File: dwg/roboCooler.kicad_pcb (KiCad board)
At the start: 2 copper layers, 82 parts, among them J1 CONN_01X02, J10 CONN_02X03, J11 CONN_02X03, J13 CONN_02X03, J14 CONN_02X03, J2 CONN_01X02, J3 CONN_02X05, J4 CONN_01X06, J5 CONN_01X12, J7 CONN_02X03, J8 CONN_02X03, Q1 NMOS, Q2 NMOS, SW1 TL3342, U1 SN74LV, U2 TB6549, U3 STM32F407VGTx, Y1 8MHz

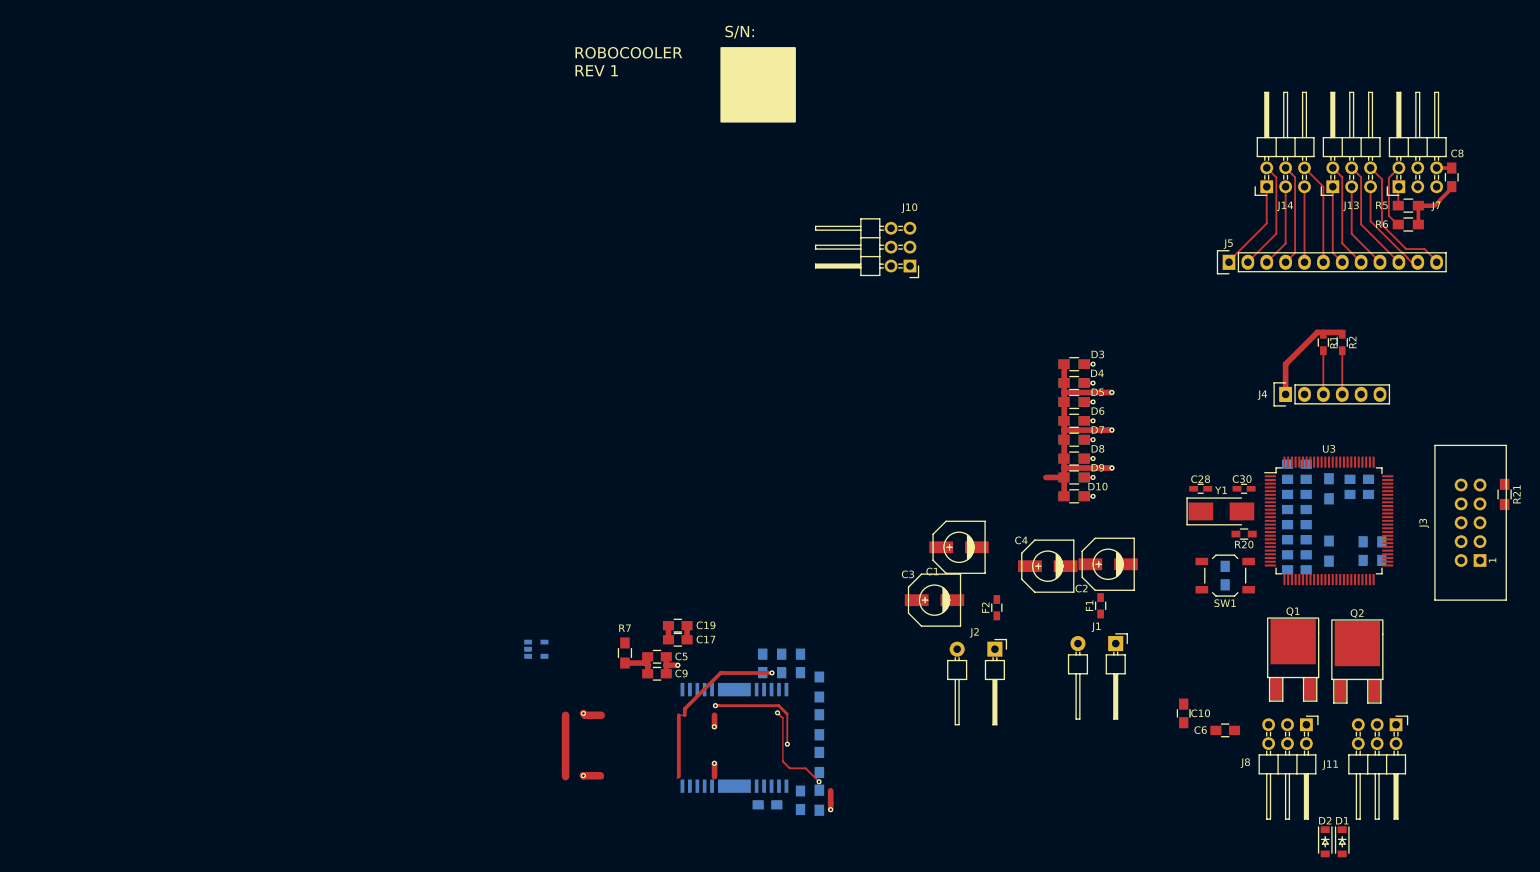
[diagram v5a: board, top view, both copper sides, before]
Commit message: updated placement on new board. No DRC errors
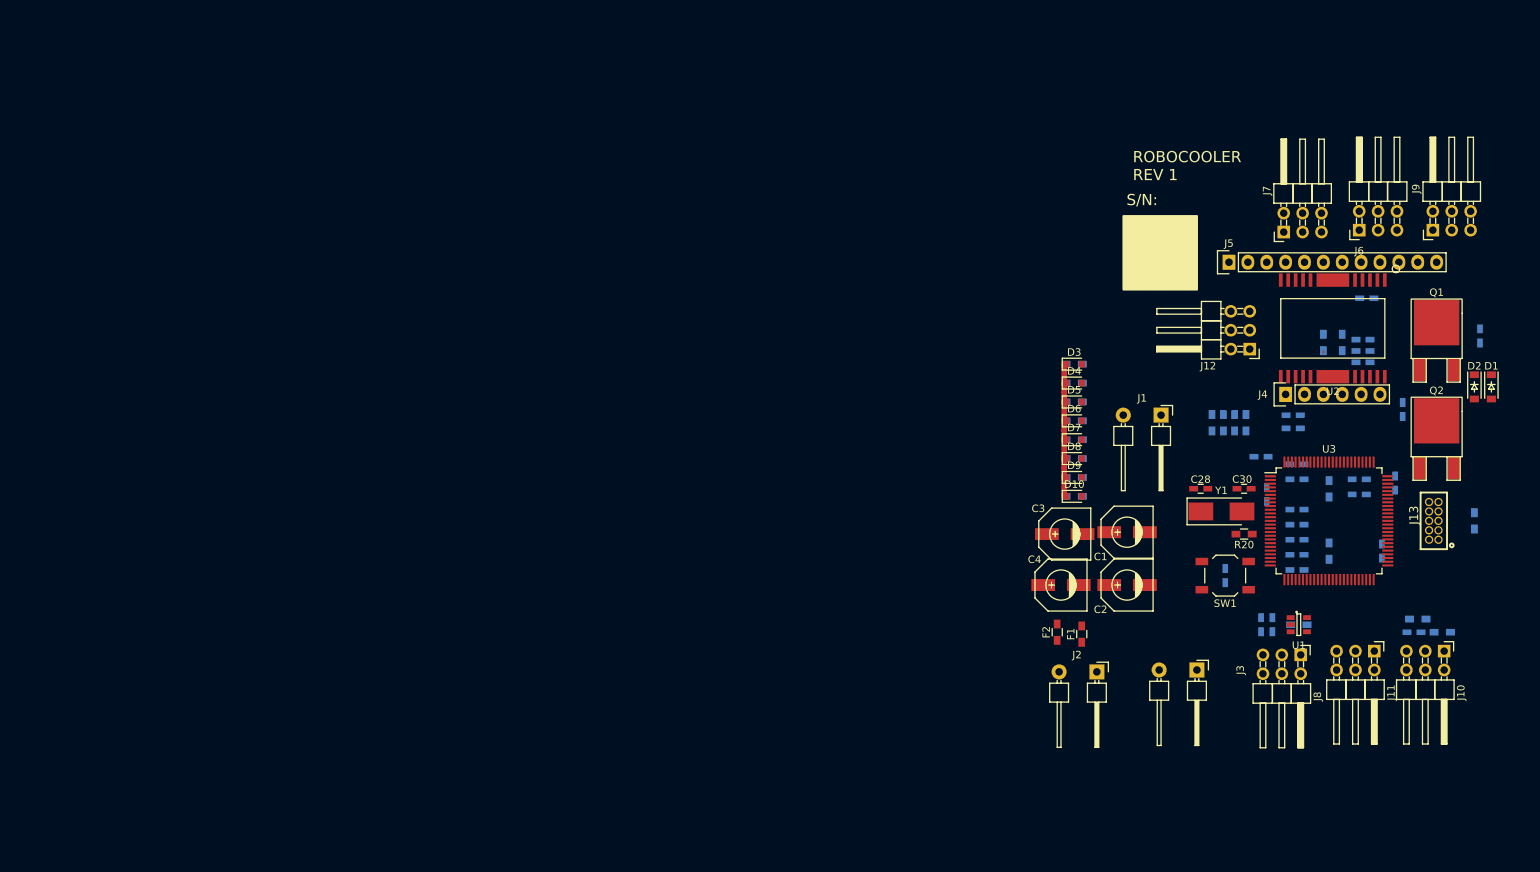
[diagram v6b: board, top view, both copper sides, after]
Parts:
- removed J14: CONN_02X03, Pin_Headers:Pin_Header_Angled_2x03
- added J12: CONN_02X03, Pin_Headers:Pin_Header_Angled_2x03_Pitch2.54mm, F.Cu at (187.7, 59.9)
- added J6: CONN_02X03, Pin_Headers:Pin_Header_Angled_2x03_Pitch2.54mm, F.Cu at (202.4, 43.9)
- added J9: CONN_02X03, Pin_Headers:Pin_Header_Angled_2x03_Pitch2.54mm, F.Cu at (212.3, 43.9)
- C1, C2, C3, C4: value 100uF -> 100UF
- C10: value 1UF -> .01UF; footprint Capacitors_SMD:C_0805_HandSoldering -> Capacitors_SMD:C_0603_HandSoldering; moved to B.Cu
- C11: value 2.2uF -> 1UF; footprint Capacitors_SMD:C_0805_HandSoldering -> Capacitors_SMD:C_0603_HandSoldering
- C12: value 10uF -> .22UF; footprint Capacitors_SMD:C_0805_HandSoldering -> Capacitors_SMD:C_0603_HandSoldering
- C13, C15: value 0.22UF -> .22UF; footprint Capacitors_SMD:C_0805_HandSoldering -> Capacitors_SMD:C_0603_HandSoldering
- C14: value 0.22UF -> .01UF; footprint Capacitors_SMD:C_0805_HandSoldering -> Capacitors_SMD:C_0603_HandSoldering
- C16, C20, C21, C22, C23, C24, C25, C26, C27, C29, C31: footprint Capacitors_SMD:C_0805_HandSoldering -> Capacitors_SMD:C_0603_HandSoldering
- C17: value .01UF -> 0.1uF; footprint Capacitors_SMD:C_0805_HandSoldering -> Capacitors_SMD:C_0603_HandSoldering; moved to B.Cu
- C18: value .01UF -> 2.2uF; footprint Capacitors_SMD:C_0805_HandSoldering -> Capacitors_SMD:C_0603_HandSoldering
- C19: value 1UF -> 10uF; footprint Capacitors_SMD:C_0805_HandSoldering -> Capacitors_SMD:C_0603_HandSoldering; moved to B.Cu
- C5: footprint Capacitors_SMD:C_0805_HandSoldering -> Capacitors_SMD:C_0603_HandSoldering; moved to B.Cu
- C6: value .01UF -> 1UF; footprint Capacitors_SMD:C_0805_HandSoldering -> Capacitors_SMD:C_0603_HandSoldering; moved to B.Cu
- C7: value 0.1uF -> .01UF; footprint Capacitors_SMD:C_0805_HandSoldering -> Capacitors_SMD:C_0603_HandSoldering
- C8: value .1UF -> 1UF; footprint Capacitors_SMD:C_0805_HandSoldering -> Capacitors_SMD:C_0603_HandSoldering; moved to B.Cu
- C9: value 1UF -> .1UF; footprint Capacitors_SMD:C_0805_HandSoldering -> Capacitors_SMD:C_0603_HandSoldering; moved to B.Cu
- D10, D3, D4, D5, D6, D7, D8, D9: value Led_Small -> LED_Small; footprint Resistors_SMD:R_0805_HandSoldering -> Diodes_SMD:D_0805
- F1, F2: value PTC -> 3.5A
- J10, J11, J7, J8: footprint Pin_Headers:Pin_Header_Angled_2x03 -> Pin_Headers:Pin_Header_Angled_2x03_Pitch2.54mm
- J13: value CONN_02X03 -> 3221-10-0100-00; footprint Pin_Headers:Pin_Header_Angled_2x03 -> roboCooler:Header_02x05_50mil
- J3: value CONN_02X05 -> CONN_01X02; footprint Connectors:IDC_Header_Straight_10pins -> roboCooler:Pin_Header_Angled_1x02_200mil
- R1, R2: value 10k -> 10K; moved to B.Cu
- R10, R8: value 10k -> 10K; footprint Resistors_SMD:R_0805_HandSoldering -> Resistors_SMD:R_0603_HandSoldering
- R11, R9: value 10k -> 200; footprint Resistors_SMD:R_0805_HandSoldering -> Resistors_SMD:R_0603_HandSoldering
- R12, R13, R14, R15, R16, R17, R18, R19: footprint Resistors_SMD:R_0805_HandSoldering -> Resistors_SMD:R_0603_HandSoldering
- R21, R5: footprint Resistors_SMD:R_0805_HandSoldering -> Resistors_SMD:R_0603_HandSoldering; moved to B.Cu
- R3: value 200 -> 1K; footprint Resistors_SMD:R_0805_HandSoldering -> Resistors_SMD:R_0603_HandSoldering
- R4: value 200 -> 1k; footprint Resistors_SMD:R_0805_HandSoldering -> Resistors_SMD:R_0603_HandSoldering
- R6, R7: value 1k -> 10K; footprint Resistors_SMD:R_0805_HandSoldering -> Resistors_SMD:R_0603_HandSoldering; moved to B.Cu
- U1: value SN74LV -> 74AHC1G14; moved to F.Cu
- U2: moved to F.Cu
- moved U1 102.7 mm to (194.3, 97.0)
- moved C9 102.0 mm to (209.8, 98.0)
- moved C13 101.8 mm to (203.5, 53.1), turned to 180 degrees
- moved C14 99.8 mm to (202.9, 61.7)
- moved U2 97.0 mm to (198.9, 57.7)
- moved C5 91.6 mm to (193.5, 68.8)
- moved C15 89.5 mm to (202.9, 58.7), turned to 180 degrees
- moved J10 88.6 mm to (213.9, 100.6), turned to 270 degrees
- moved C18 88.5 mm to (207.3, 78.0)
- moved C16 86.6 mm to (202.9, 60.2), turned to 180 degrees
- moved R7 86.3 mm to (184.2, 69.8), turned to 270 degrees
- moved C19 81.7 mm to (189.2, 74.4)
- moved C17 81.6 mm to (190.0, 79.5), turned to 90 degrees
- moved R10 73.4 mm to (187.2, 69.8), turned to 270 degrees
- moved R8 66.2 mm to (185.7, 69.8)
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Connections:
- net JTRST renamed Net-(U3-Pad90)
- C11 pad 1: Net-(C11-Pad1) -> +12V
- C12 pad 1: VDD -> Net-(C12-Pad1)
- C13 pad 2: GND -> Net-(C13-Pad2)
- C14 pad 2: Net-(C14-Pad2) -> GND
- C15 pad 1: GND -> +12V
- C15 pad 2: +12V -> GND
- C16 pad 1: GND -> +12V
- C16 pad 2: +12V -> GND
- C17 pad 1: +3V3 -> VCC
- C18 pad 1: Net-(C18-Pad1) -> VCAP_2
- C19 pad 1: +3V3 -> VCC
- C20 pad 1: Net-(C20-Pad1) -> VCAP_1
- C22 pad 1: VDD -> VCC
- C23 pad 1: VDD -> VCC
- C24 pad 1: VDD -> VCC
- C25 pad 1: VDD -> VCC
- C26 pad 1: VDD -> VCC
- C27 pad 1: VDD -> VCC
- C5 pad 1: +5V -> +3V3
- C6 pad 1: +12V -> +3V3
- C7 pad 1: VDD -> +5V
- C8 pad 1: +5P -> +5V
- J1 pad 1: Net-(F1-Pad1) -> +3V3
- J10 pad 1: +5V -> Net-(J10-Pad1)
- J10 pad 2: +5V -> Net-(J10-Pad2)
- J10 pad 3: Net-(J10-Pad3) -> HALL_1
- J10 pad 4: Net-(J10-Pad3) -> HALL_2
- J11 pad 1: MOTOR_OUT1 -> Net-(J11-Pad1)
- J11 pad 2: MOTOR_OUT1 -> Net-(J11-Pad2)
- J11 pad 3: GND -> PUSH_1
- J11 pad 4: GND -> PUSH_2
- J11 pad 5: MOTOR_OUT2 -> GND
- J11 pad 6: MOTOR_OUT2 -> GND
- J13 pad 1: CS_5 -> VCC
- J13 pad 2: CS_4 -> JTMS/SWDIO
- J13 pad 3: CS_3 -> GND
- J13 pad 4: CS_2 -> JTCK/SWCLK
- J13 pad 5: CS_1 -> GND
- J13 pad 6: CS_0 -> JTDO/SWO
- J2 pad 1: Net-(F2-Pad1) -> Net-(F1-Pad1)
- J3 pad 1: VCC -> Net-(F2-Pad1)
- J3 pad 2: JTMS/SWDIO -> GND
- J7 pad 1: Net-(J7-Pad1) -> CS_11
- J7 pad 2: Net-(J7-Pad2) -> CS_10
- J7 pad 3: HALL_1 -> CS_9
- J7 pad 4: HALL_2 -> CS_8
- J7 pad 5: GND -> CS_7
- J7 pad 6: GND -> CS_6
- J8 pad 1: +12V -> +5V
- J8 pad 2: +12V -> +5V
- J8 pad 4: Net-(J8-Pad4) -> Net-(J8-Pad3)
- J8 pad 5: Net-(D1-Pad2) -> GND
- J8 pad 6: Net-(D2-Pad2) -> GND
- R10 pad 1: GND -> MOTOR_SB
- R10 pad 2: MOTOR_PWM -> GND
- R11 pad 1: GND -> LED_1
- R11 pad 2: MOTOR_SB -> Net-(D4-Pad2)
- R21 pad 2: Net-(J3-Pad7) -> Net-(J13-Pad7)
- R3 pad 1: LED_0 -> +5V
- R3 pad 2: Net-(D3-Pad2) -> Net-(J8-Pad3)
- R4 pad 1: LED_1 -> Net-(J10-Pad1)
- R4 pad 2: Net-(D4-Pad2) -> +5V
- R5 pad 1: Net-(J7-Pad1) -> +5V
- R5 pad 2: +5P -> Net-(J10-Pad2)
- R6 pad 1: Net-(J7-Pad2) -> MOTOR_FWD
- R6 pad 2: +5P -> GND
- R7 pad 1: +5V -> MOTOR_REV
- R7 pad 2: Net-(J10-Pad3) -> GND
- R8 pad 1: GND -> MOTOR_PWM
- R8 pad 2: MOTOR_IN1 -> GND
- R9 pad 1: GND -> LED_0
- R9 pad 2: MOTOR_IN2 -> Net-(D3-Pad2)
- U1 pad 4: Net-(J10-Pad3) -> Net-(J8-Pad3)
- U2 pad 18: Net-(C18-Pad1) -> Net-(C14-Pad1)
- U2 pad 2: Net-(C13-Pad1) -> Net-(C12-Pad1)
- U2 pad 3: Net-(C14-Pad1) -> Net-(C13-Pad1)
- U2 pad 4: Net-(C14-Pad2) -> Net-(C13-Pad2)
- U2 pad 7: MOTOR_IN1 -> MOTOR_FWD
- U2 pad 8: MOTOR_IN2 -> MOTOR_REV
- U3 pad 100: VDD -> VCC
- U3 pad 11: VDD -> VCC
- U3 pad 19: VDD -> VCC
- U3 pad 24: /mcu/LED_1 -> LED_1
- U3 pad 25: /mcu/LED_UART -> LED_UART
- U3 pad 26: /mcu/LED_2 -> LED_2
- U3 pad 28: VDD -> VCC
- U3 pad 32: /mcu/LED_3 -> LED_3
- U3 pad 34: /mcu/LED_4 -> LED_4
- U3 pad 36: /mcu/LED_5 -> LED_5
- U3 pad 38: /mcu/LED_6 -> LED_6
- U3 pad 4: /mcu/PUSH_1 -> PUSH_1
- U3 pad 40: /mcu/LED_7 -> LED_7
- U3 pad 49: Net-(C11-Pad1) -> VCAP_1
- U3 pad 50: VDD -> VCC
- U3 pad 6: VDD -> VCC
- U3 pad 63: /mcu/FAN_PWM -> FAN
- U3 pad 66: /mcu/PUMP_PWM -> PUMP
- U3 pad 67: /mcu/MOTOR_PWM -> MOTOR_PWM
- U3 pad 7: /mcu/PUSH_2 -> PUSH_2
- U3 pad 73: Net-(C20-Pad1) -> VCAP_2
- U3 pad 75: VDD -> VCC
- U3 pad 79: /mcu/MOTOR_REV -> MOTOR_REV
- U3 pad 81: /mcu/MOTOR_FWD -> MOTOR_FWD
- U3 pad 83: /mcu/MOTOR_SB -> MOTOR_SB
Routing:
- net (no net): track 70.1 -> 0.12 mm, vias 10 -> 0
- net GND: track 47.3 -> 17.8 mm, vias 4 -> 0
- net CS_0: track 17.8 -> 0.15 mm
- net +3V3: track 15.4 -> 0.00 mm
- net CS_2: track 15.3 -> 0.01 mm
- net CS_10: track 14.8 -> 0.01 mm
- net CS_4: track 14.3 -> 0.00 mm
- net CS_6: track 13.8 -> 0.00 mm
- net CS_8: track 13.8 -> 0.02 mm
- net CS_1: track 13.3 -> 0.83 mm
- net CS_11: track 12.3 -> 0.15 mm
- net CS_3: track 11.7 -> 0.01 mm
- net CS_9: track 11.2 -> 0.02 mm
- net CS_5: track 10.7 -> 0.00 mm
- net +5P: track 10.2 -> 0.00 mm
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
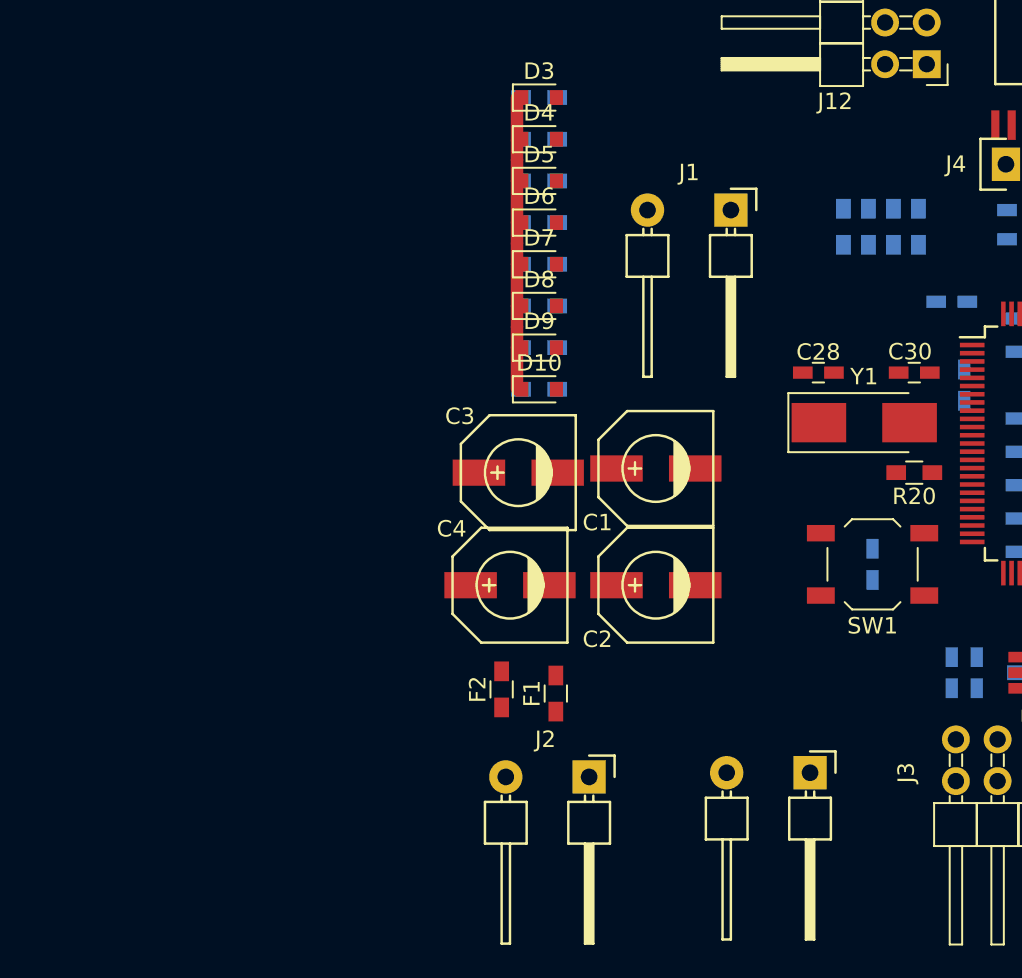
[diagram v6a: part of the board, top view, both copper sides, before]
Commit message: added 5V switcher
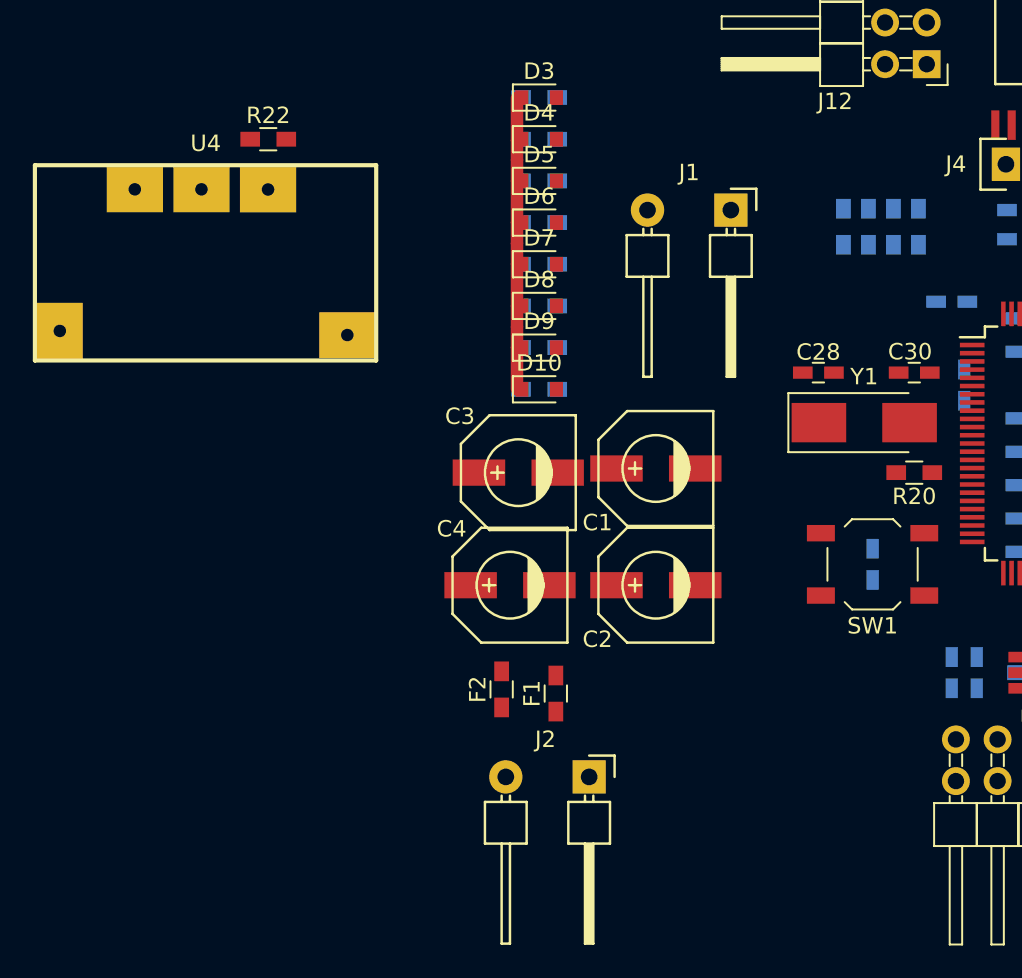
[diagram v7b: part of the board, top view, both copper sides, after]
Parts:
- removed J3: CONN_01X02, roboCooler:Pin_Header_Angled_1x02_200mil
- added R22: 10K, Resistors_SMD:R_0603_HandSoldering, F.Cu at (147.6, 64.5)
- added U4: OKY-T/3-D12N-C, roboCooler:OKY-T3, F.Cu at (134.9, 76.2)
- F2: value 3.5A -> 5A
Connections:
- C2 pad 1: +5V -> Net-(C2-Pad1)
- C4 pad 1: +5V -> Net-(C2-Pad1)
- F2 pad 1: Net-(F2-Pad1) -> +5V
- F2 pad 2: +5V -> Net-(C2-Pad1)
- J11 pad 3: PUSH_1 -> Net-(J11-Pad3)
- J11 pad 4: PUSH_2 -> Net-(J11-Pad4)
- J11 pad 5: GND -> Net-(J11-Pad5)
- J11 pad 6: GND -> Net-(J11-Pad6)

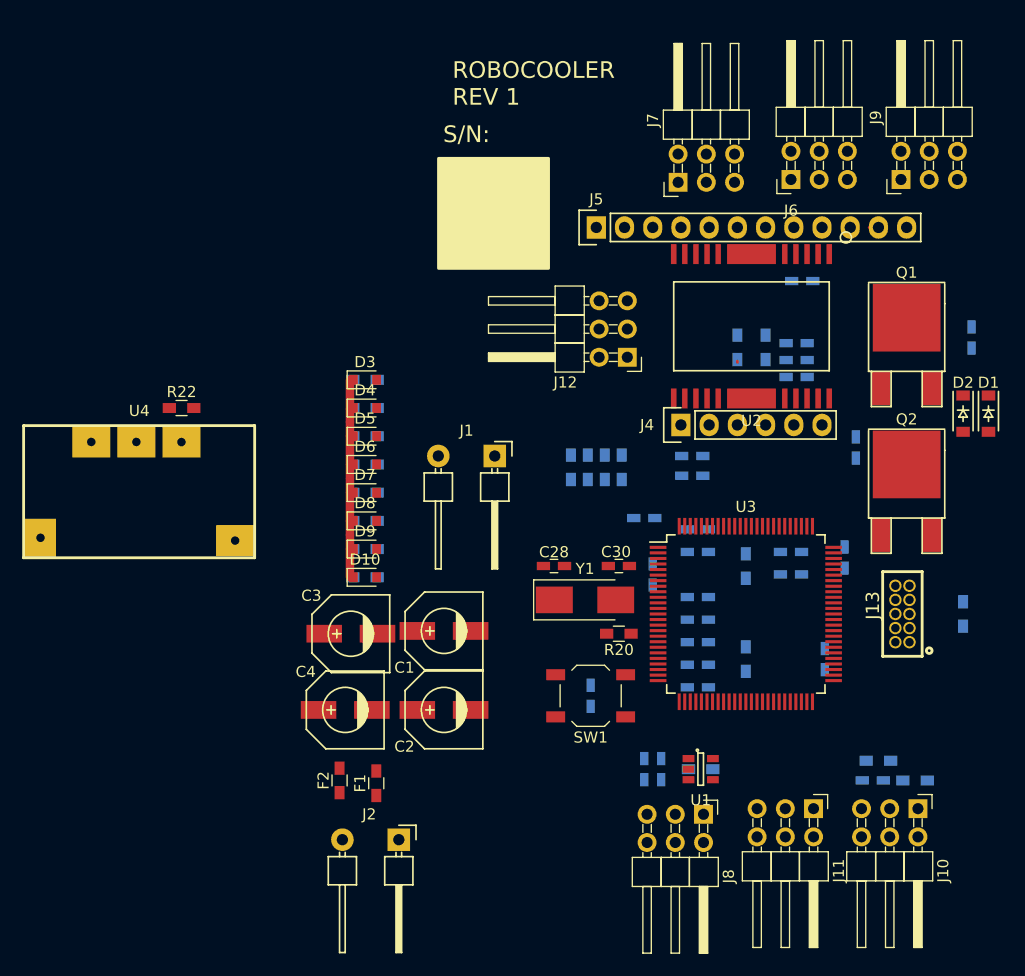
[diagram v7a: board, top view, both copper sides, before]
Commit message: added 3.3V LDO
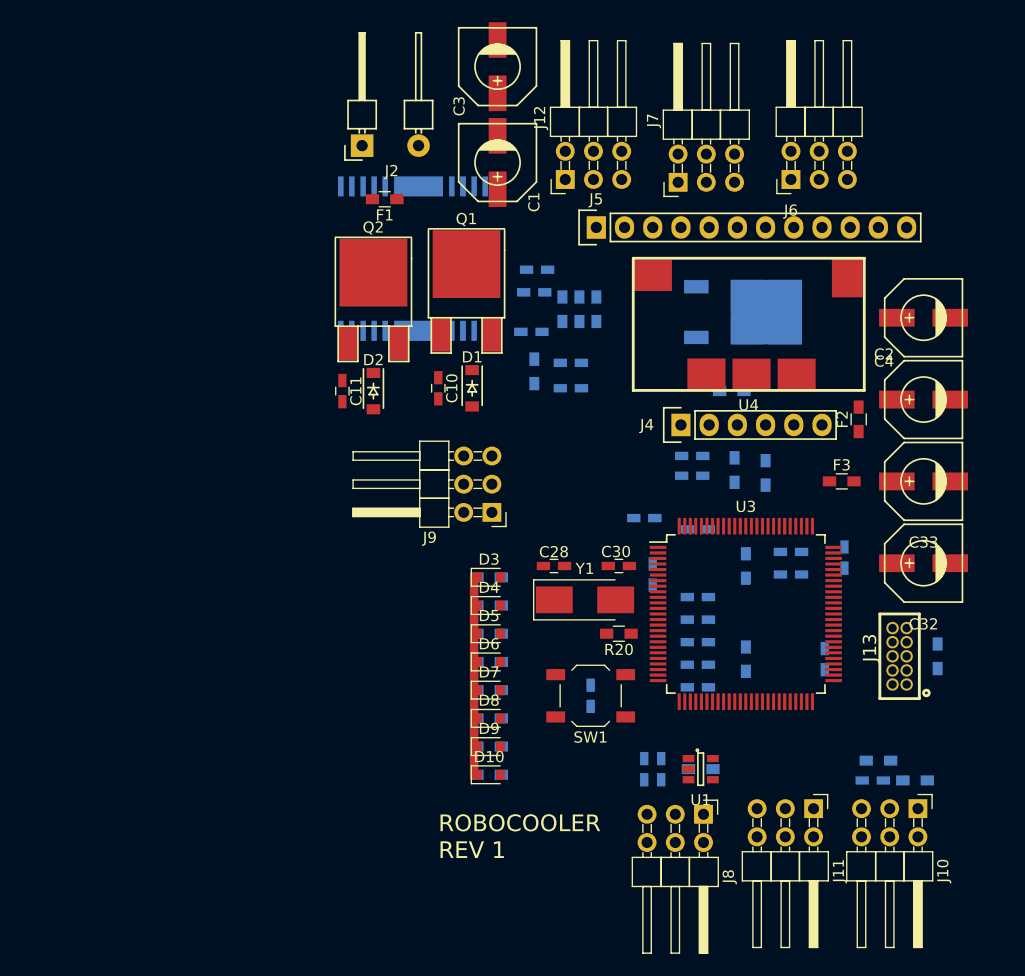
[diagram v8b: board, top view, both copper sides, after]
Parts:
- removed J1: CONN_01X02, roboCooler:Pin_Header_Angled_1x02_200mil
- added C32: 100UF, roboCooler:c_elec_6.6x6.6, F.Cu at (214.4, 78.5)
- added C33: 100UF, roboCooler:c_elec_6.6x6.6, F.Cu at (214.4, 71.1)
- added F3: 1A, Resistors_SMD:R_0603_HandSoldering, F.Cu at (207.0, 71.1)
- added U5: NCP1117DT33G, TO_SOT_Packages_SMD:TO-252-2, B.Cu at (198.1, 55.9)
- C10, C11: moved to F.Cu
- R22: value 10K -> 1.472K; moved to B.Cu
- U2: moved to B.Cu
- moved U4 76.3 mm to (207.5, 52.8), turned to 180 degrees
- moved J2 62.5 mm to (166.4, 40.9), turned to 90 degrees
- moved C4 59.1 mm to (214.4, 63.8)
- moved F2 56.9 mm to (208.5, 65.5)
- moved C2 55.8 mm to (214.4, 56.4)
- moved D2 53.1 mm to (164.8, 63.0)
- moved C3 52.7 mm to (176.0, 33.8), turned to 270 degrees
- moved F1 52.6 mm to (165.9, 45.7), turned to 180 degrees
- moved Q2 51.0 mm to (164.8, 58.7)
- moved R22 49.6 mm to (197.1, 63.0), turned to 180 degrees
- moved C10 48.2 mm to (170.7, 62.7)
- moved J9 47.5 mm to (175.5, 73.9), turned to 180 degrees
- moved D1 46.5 mm to (173.7, 62.7)
- moved C11 46.5 mm to (162.1, 63.0), turned to 270 degrees
- moved C1 42.4 mm to (176.0, 42.4), turned to 270 degrees
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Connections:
- C2 pad 1: Net-(C2-Pad1) -> +5V
- C4 pad 1: Net-(C2-Pad1) -> +5V
- F2 pad 1: +5V -> Net-(F2-Pad1)
- F2 pad 2: Net-(C2-Pad1) -> +5V
- J11 pad 3: Net-(J11-Pad3) -> PUSH_1
- J11 pad 4: Net-(J11-Pad4) -> PUSH_2
- J11 pad 5: Net-(J11-Pad5) -> GND
- J11 pad 6: Net-(J11-Pad6) -> GND
- U4 pad 5: +5V -> Net-(F2-Pad1)
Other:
- board text removed: "S/N:"
